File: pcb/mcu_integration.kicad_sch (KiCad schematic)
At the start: 32 parts, among them J5 DM3BT-DSF-PEJS, M1 MountingHole_Pad, M2 MountingHole_Pad, M3 MountingHole_Pad, M4 MountingHole_Pad, U1 STM32F103RBTx, U6 LM35DM, Y1 ECS-80-18-5PX-GM-TR

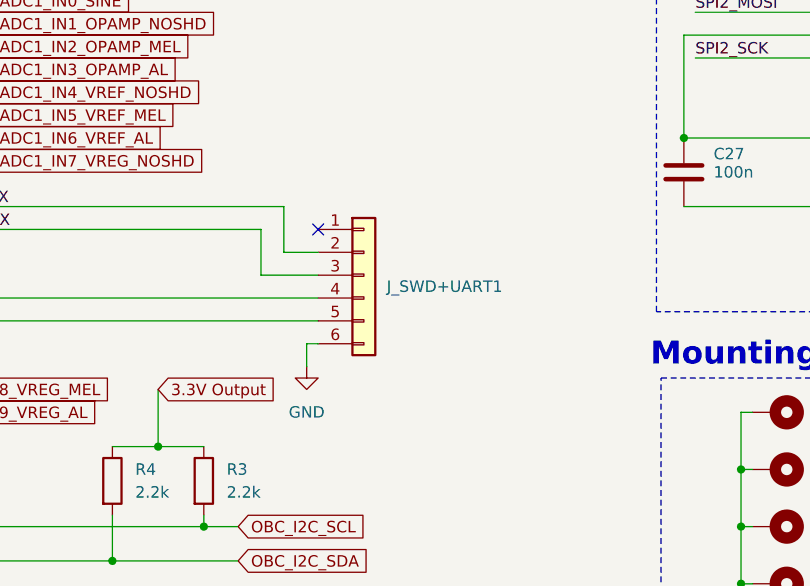
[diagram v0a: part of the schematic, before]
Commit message: Added non-inverting amplifier to RC Ladder and Changed header pin
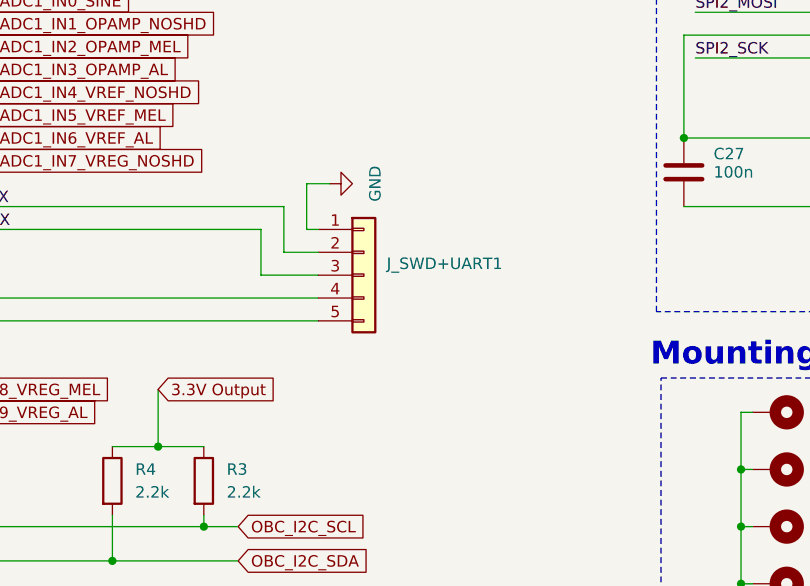
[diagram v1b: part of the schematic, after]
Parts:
- removed J_SWD+UART1: Conn_01x06, Connector_PinHeader_2.54mm:PinHeader_1x06_P2.54mm_Vertical, symbol Connector_Generic:Conn_01x06
- added J_SWD+UART1: J_SWD+UART1, Connector_PinHeader_2.54mm:PinHeader_1x05_P2.54mm_Vertical, symbol Connector_Generic:Conn_01x05
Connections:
- net GND: now also J_SWD+UART1.1 (Pin_1)
- net SWCLK: now also J_SWD+UART1.5 (Pin_5)
- net SWDIO: now also J_SWD+UART1.4 (Pin_4)
- net USART1_RX: now also J_SWD+UART1.3 (Pin_3)
- net USART1_TX: now also J_SWD+UART1.2 (Pin_2)
- no-connect marks 31 -> 30
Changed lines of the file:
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@@
 	)
 	(no_connect
-		(at 163.83 62.23)
-	)
-	(no_connect
 		(at 116.84 105.41)
 	)
@@
 	(wire
 		(pts
-			(xy 162.56 74.93) (xy 163.83 74.93)
-		)
-		(stroke
-			(width 0)
-			(type default)
-		)
-	)
-	(wire
-		(pts
 			(xy 60.96 134.62) (xy 77.47 134.62)
 		)
@@
 	(wire
 		(pts
-			(xy 162.56 77.47) (xy 162.56 74.93)
+			(xy 165.1 57.15) (xy 162.56 57.15)
 		)
 		(stroke
@@
 	(wire
 		(pts
+			(xy 162.56 57.15) (xy 162.56 62.23)
+		)
+		(stroke
+			(width 0)
+			(type default)
+		)
+	)
+	(wire
+		(pts
 			(xy 210.82 82.55) (xy 212.09 82.55)
 		)
@@
 	(wire
 		(pts
+			(xy 163.83 62.23) (xy 162.56 62.23)
+		)
+		(stroke
+			(width 0)
+			(type default)
+		)
+	)
+	(wire
+		(pts
 			(xy 96.52 30.48) (xy 99.06 30.48)
 		)
@@
 	(label "SPI2_SCK"
 		(at 205.74 43.18 0)
-		(fields_autoplaced yes)
 		(effects
 			(font
@@
 	(label "SPI2_CS_NSS"
 		(at 205.74 35.56 0)
-		(fields_autoplaced yes)
 		(effects
 			(font
@@
 	(label "HSE_OSC_OUT"
 		(at 67.31 49.53 0)
-		(fields_autoplaced yes)
 		(effects
 			(font
@@
 	(label "USART1_TX"
 		(at 119.38 59.69 0)
-		(fields_autoplaced yes)
 		(effects
 			(font
@@
 	(label "HSE_OSC_IN"
 		(at 67.31 46.99 0)
-		(fields_autoplaced yes)
 		(effects
 			(font
@@
 	(label "SPI2_CS_NSS"
 		(at 119.38 110.49 0)
-		(fields_autoplaced yes)
 		(effects
 			(font
@@
 	(label "SPI2_MOSI"
 		(at 205.74 38.1 0)
-		(fields_autoplaced yes)
 		(effects
 			(font
@@
 	(label "SPI2_MOSI"
 		(at 119.38 118.11 0)
-		(fields_autoplaced yes)
 		(effects
 			(font
@@
 	(label "SPI2_MISO"
 		(at 119.38 115.57 0)
-		(fields_autoplaced yes)
 		(effects
 			(font
@@
 	(label "SWCLK"
 		(at 119.38 72.39 0)
-		(fields_autoplaced yes)
 		(effects
 			(font
@@
 	(label "USART1_RX"
 		(at 119.38 62.23 0)
-		(fields_autoplaced yes)
 		(effects
 			(font
@@
 	(label "SPI2_MISO"
 		(at 276.86 40.64 180)
-		(fields_autoplaced yes)
 		(effects
 			(font
@@
 	(label "BOOT0"
 		(at 68.58 40.64 0)
-		(fields_autoplaced yes)
 		(effects
 			(font
@@
 	(label "NRST"
 		(at 73.66 36.83 0)
-		(fields_autoplaced yes)
 		(effects
 			(font
@@
 	(label "SWDIO"
 		(at 119.38 69.85 0)
-		(fields_autoplaced yes)
 		(effects
 			(font
@@
 	(label "SPI2_SCK"
 		(at 119.38 113.03 0)
-		(fields_autoplaced yes)
 		(effects
 			(font
@@
 	)
 	(symbol
-		(lib_id "Connector_Generic:Conn_01x06")
-		(at 168.91 67.31 0)
-		(unit 1)
-		(exclude_from_sim no)
-		(in_bom yes)
-		(on_board yes)
-		(dnp no)
-		(fields_autoplaced yes)
-		(property "Reference" "J_SWD+UART1"
-			(at 171.45 68.58 0)
-			(effects
-				(font
-					(size 1.27 1.27)
-				)
-				(justify left)
-			)
-		)
-		(property "Value" "Conn_01x06"
-			(at 171.45 69.85 0)
-			(effects
-				(font
-					(size 1.27 1.27)
-				)
-				(justify left)
-				(hide yes)
-			)
-		)
-		(property "Footprint" "Connector_PinHeader_2.54mm:PinHeader_1x06_P2.54mm_Vertical"
-			(at 168.91 67.31 0)
-			(effects
-				(font
-					(size 1.27 1.27)
-				)
-				(hide yes)
-			)
-		)
-		(property "Datasheet" "~"
-			(at 168.91 67.31 0)
-			(effects
-				(font
-					(size 1.27 1.27)
-				)
-				(hide yes)
-			)
-		)
-		(property "Description" ""
-			(at 168.91 67.31 0)
-			(effects
-				(font
-					(size 1.27 1.27)
-				)
-				(hide yes)
-			)
-		)
-		(pin "1"
-		)
-		(pin "2"
-		)
-		(pin "3"
-		)
-		(pin "4"
-		)
-		(pin "5"
-		)
-		(pin "6"
-		)
-		(instances
-			(project "mcu_integration"
-				(path "/c0210bc3-f67f-47d8-a34e-f002a728adb2"
-					(reference "J_SWD+UART1")
-					(unit 1)
-				)
-			)
-		)
-	)
-	(symbol
 		(lib_id "Device:C")
 		(at 49.53 62.23 180)
@@
 	(symbol
 		(lib_id "power:GND")
-		(at 162.56 77.47 0)
+		(at 165.1 57.15 90)
 		(unit 1)
 		(exclude_from_sim no)
@@
 		(fields_autoplaced yes)
 		(property "Reference" "#PWR013"
-			(at 162.56 83.82 0)
+			(at 171.45 57.15 0)
 			(effects
 				(font
@@
 		)
 		(property "Value" "GND"
-			(at 162.56 82.55 0)
+			(at 170.18 57.15 0)
 			(effects
 				(font
@@
 		)
 		(property "Footprint" ""
-			(at 162.56 77.47 0)
+			(at 165.1 57.15 0)
 			(effects
 				(font
@@
 		)
 		(property "Datasheet" ""
-			(at 162.56 77.47 0)
+			(at 165.1 57.15 0)
 			(effects
 				(font
@@
 		)
 		(property "Description" ""
-			(at 162.56 77.47 0)
+			(at 165.1 57.15 0)
 			(effects
 				(font
@@
 					(unit 1)
 				)
+			)
+		)
+	)
+	(symbol
+		(lib_id "Connector_Generic:Conn_01x05")
+		(at 168.91 67.31 0)
+		(unit 1)
+		(exclude_from_sim no)
+		(in_bom yes)
+		(on_board yes)
+		(dnp no)
+		(property "Reference" "J_SWD+UART1"
+			(at 171.45 66.0399 0)
+			(effects
+				(font
+					(size 1.27 1.27)
+				)
+				(justify left)
+			)
+		)
+		(property "Value" "J_SWD+UART1"
+			(at 171.45 68.58 0)
+			(effects
+				(font
+					(size 1.27 1.27)
+				)
+				(justify left)
+				(hide yes)
+			)
+		)
+		(property "Footprint" "Connector_PinHeader_2.54mm:PinHeader_1x05_P2.54mm_Vertical"
+			(at 168.91 67.31 0)
+			(effects
+				(font
+					(size 1.27 1.27)
+				)
+				(hide yes)
+			)
+		)
+		(property "Datasheet" "~"
+			(at 168.91 67.31 0)
+			(effects
+				(font
+					(size 1.27 1.27)
+				)
+				(hide yes)
+			)
+		)
+		(property "Description" "Generic connector, single row, 01x05, script generated (kicad-library-utils/schlib/autogen/connector/)"
+			(at 168.91 67.31 0)
+			(effects
+				(font
+					(size 1.27 1.27)
+				)
+				(hide yes)
+			)
+		)
+		(pin "1"
+		)
+		(pin "3"
+		)
+		(pin "4"
+		)
+		(pin "2"
+		)
+		(pin "5"
+		)
+		(instances
+			(project "mcu_integration"
+				(path "/c0210bc3-f67f-47d8-a34e-f002a728adb2"
+					(reference "J_SWD+UART1")
+					(unit 1)
+				)

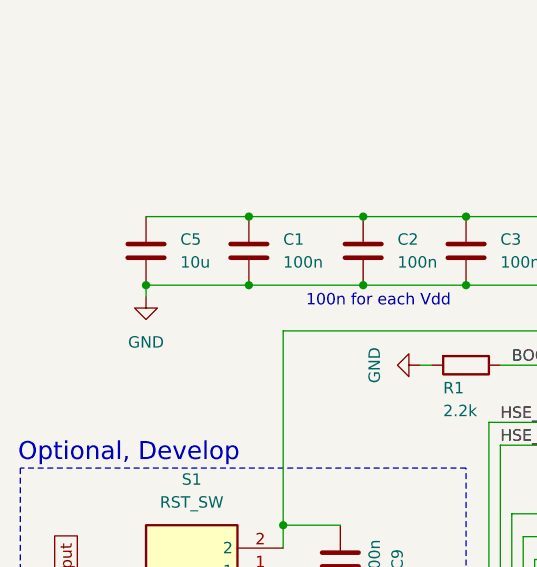
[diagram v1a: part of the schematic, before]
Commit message: Added missing decoupling capacitor + changed capacitors footprint
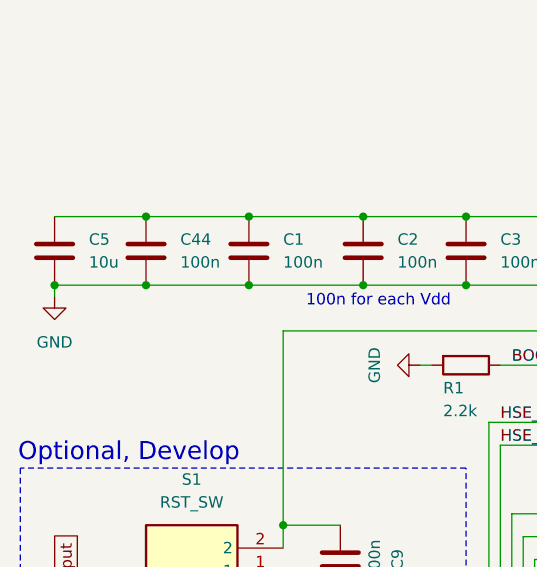
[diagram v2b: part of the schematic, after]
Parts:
- added C44: 100n, Capacitor_SMD:C_0402_1005Metric, symbol Device:C
- C1: footprint Resistor_SMD:R_0402_1005Metric -> Capacitor_SMD:C_0402_1005Metric
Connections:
- net 3.3V Output: now also C44.1
- net GND: now also C44.2
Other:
- moved on the sheet: C5
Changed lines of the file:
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@@
 	)
 	(junction
+		(at 27.94 31.75)
+		(diameter 0)
+		(color 0 0 0 0)
+	)
+	(junction
 		(at 151.13 95.25)
 		(diameter 0)
@@
 	)
 	(junction
-		(at 154.94 20.32)
+		(at 27.94 24.13)
 		(diameter 0)
 		(color 0 0 0 0)
 	)
 	(junction
-		(at 27.94 31.75)
+		(at 154.94 20.32)
 		(diameter 0)
 		(color 0 0 0 0)
@@
 	)
 	(junction
+		(at 17.78 31.75)
+		(diameter 0)
+		(color 0 0 0 0)
+	)
+	(junction
 		(at 44.45 95.25)
 		(diameter 0)
@@
 	(wire
 		(pts
-			(xy 27.94 31.75) (xy 39.37 31.75)
-		)
-		(stroke
-			(width 0)
-			(type default)
-		)
-	)
-	(wire
-		(pts
 			(xy 43.18 63.5) (xy 43.18 66.04)
 		)
@@
 	(wire
 		(pts
-			(xy 27.94 31.75) (xy 27.94 33.02)
+			(xy 17.78 31.75) (xy 17.78 33.02)
 		)
 		(stroke
@@
 	(wire
 		(pts
+			(xy 27.94 31.75) (xy 39.37 31.75)
+		)
+		(stroke
+			(width 0)
+			(type default)
+		)
+	)
+	(wire
+		(pts
 			(xy 160.02 64.77) (xy 163.83 64.77)
 		)
@@
 	(wire
 		(pts
-			(xy 27.94 24.13) (xy 39.37 24.13)
+			(xy 17.78 24.13) (xy 27.94 24.13)
 		)
 		(stroke
@@
 	(wire
 		(pts
+			(xy 27.94 24.13) (xy 39.37 24.13)
+		)
+		(stroke
+			(width 0)
+			(type default)
+		)
+	)
+	(wire
+		(pts
 			(xy 163.83 62.23) (xy 162.56 62.23)
 		)
@@
 	(wire
 		(pts
+			(xy 17.78 31.75) (xy 27.94 31.75)
+		)
+		(stroke
+			(width 0)
+			(type default)
+		)
+	)
+	(wire
+		(pts
 			(xy 204.47 52.07) (xy 222.25 52.07)
 		)
@@
 	(symbol
 		(lib_id "Device:C")
-		(at 27.94 27.94 0)
+		(at 17.78 27.94 0)
 		(unit 1)
 		(exclude_from_sim no)
@@
 		(fields_autoplaced yes)
 		(property "Reference" "C5"
-			(at 31.75 26.67 0)
+			(at 21.59 26.67 0)
 			(effects
 				(font
@@
 		)
 		(property "Value" "10u"
-			(at 31.75 29.21 0)
+			(at 21.59 29.21 0)
 			(effects
 				(font
@@
 		)
 		(property "Footprint" "Capacitor_SMD:C_0603_1608Metric"
-			(at 28.9052 31.75 0)
+			(at 18.7452 31.75 0)
 			(effects
 				(font
@@
 		)
 		(property "Datasheet" "~"
-			(at 27.94 27.94 0)
+			(at 17.78 27.94 0)
 			(effects
 				(font
@@
 		)
 		(property "Description" ""
-			(at 27.94 27.94 0)
+			(at 17.78 27.94 0)
 			(effects
 				(font
@@
 	(symbol
 		(lib_id "Device:C")
+		(at 27.94 27.94 0)
+		(unit 1)
+		(exclude_from_sim no)
+		(in_bom yes)
+		(on_board yes)
+		(dnp no)
+		(fields_autoplaced yes)
+		(property "Reference" "C44"
+			(at 31.75 26.67 0)
+			(effects
+				(font
+					(size 1.27 1.27)
+				)
+				(justify left)
+			)
+		)
+		(property "Value" "100n"
+			(at 31.75 29.21 0)
+			(effects
+				(font
+					(size 1.27 1.27)
+				)
+				(justify left)
+			)
+		)
+		(property "Footprint" "Capacitor_SMD:C_0402_1005Metric"
+			(at 28.9052 31.75 0)
+			(effects
+				(font
+					(size 1.27 1.27)
+				)
+				(hide yes)
+			)
+		)
+		(property "Datasheet" "~"
+			(at 27.94 27.94 0)
+			(effects
+				(font
+					(size 1.27 1.27)
+				)
+				(hide yes)
+			)
+		)
+		(property "Description" ""
+			(at 27.94 27.94 0)
+			(effects
+				(font
+					(size 1.27 1.27)
+				)
+				(hide yes)
+			)
+		)
+		(pin "1"
+		)
+		(pin "2"
+		)
+		(instances
+			(project "mcu_integration"
+				(path "/c0210bc3-f67f-47d8-a34e-f002a728adb2"
+					(reference "C44")
+					(unit 1)
+				)
+			)
+		)
+	)
+	(symbol
+		(lib_id "Device:C")
 		(at 76.2 27.94 0)
 		(unit 1)
@@
 			)
 		)
-		(property "Footprint" "Resistor_SMD:R_0402_1005Metric"
+		(property "Footprint" "Capacitor_SMD:C_0402_1005Metric"
 			(at 40.3352 31.75 0)
 			(effects
@@
 	(symbol
 		(lib_id "power:GND")
-		(at 27.94 33.02 0)
+		(at 17.78 33.02 0)
 		(unit 1)
 		(exclude_from_sim no)
@@
 		(fields_autoplaced yes)
 		(property "Reference" "#PWR03"
-			(at 27.94 39.37 0)
+			(at 17.78 39.37 0)
 			(effects
 				(font
@@
 		)
 		(property "Value" "GND"
-			(at 27.94 38.1 0)
+			(at 17.78 38.1 0)
 			(effects
 				(font
@@
 		)
 		(property "Footprint" ""
-			(at 27.94 33.02 0)
+			(at 17.78 33.02 0)
 			(effects
 				(font
@@
 		)
 		(property "Datasheet" ""
-			(at 27.94 33.02 0)
+			(at 17.78 33.02 0)
 			(effects
 				(font
@@
 		)
 		(property "Description" ""
-			(at 27.94 33.02 0)
+			(at 17.78 33.02 0)
 			(effects
 				(font

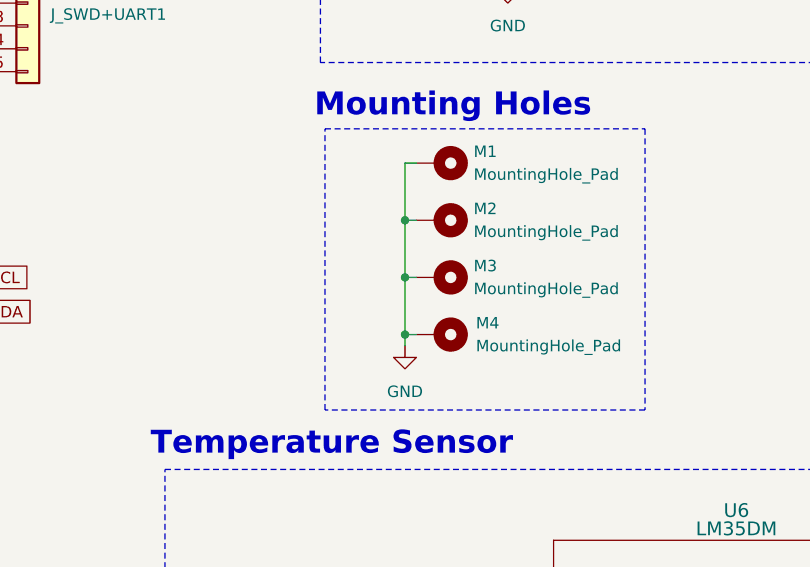
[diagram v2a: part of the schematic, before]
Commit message: Added copper pours to top and bottom layer, added 3.3v plane, spaced ICs to fit melanin caps, ungrounded connection pads, added stitching vias to outer edge
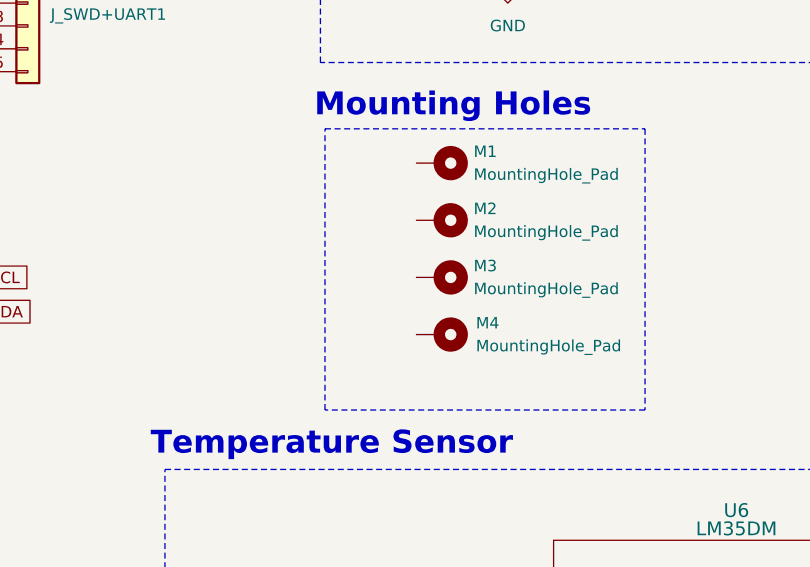
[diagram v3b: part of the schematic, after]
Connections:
- net GND: no longer M1.1, M2.1, M3.1, M4.1

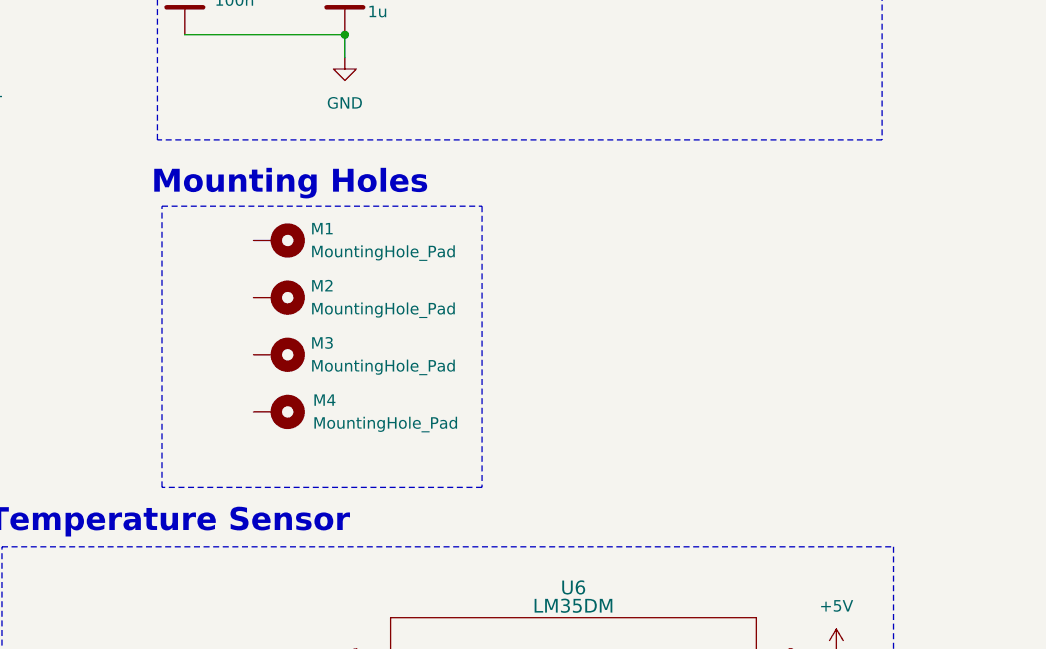
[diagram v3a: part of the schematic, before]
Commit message: Added Shield Footprints
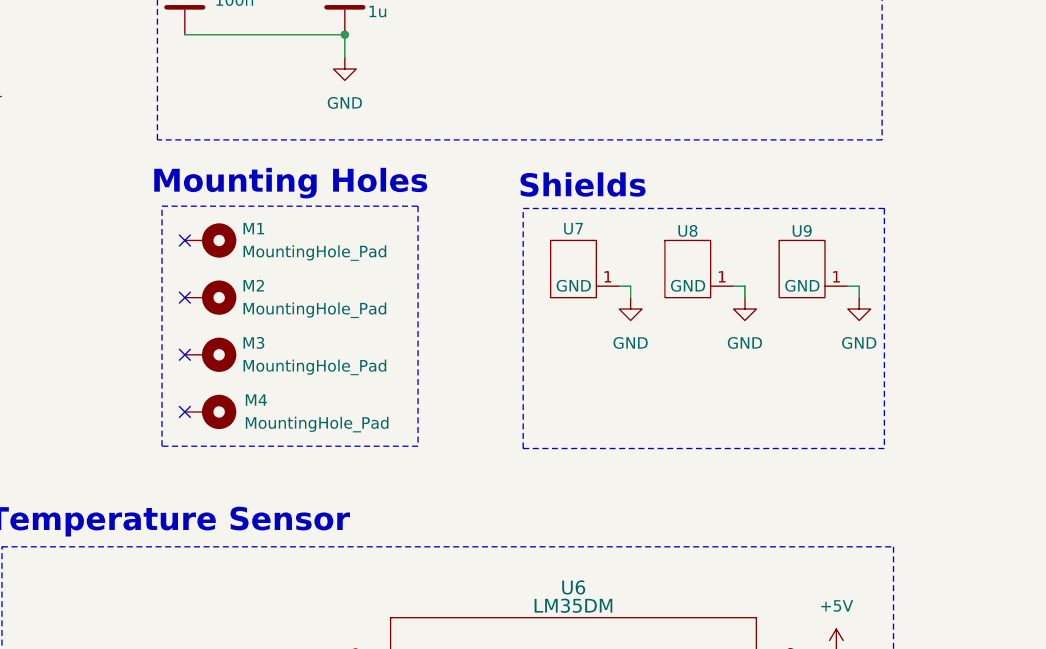
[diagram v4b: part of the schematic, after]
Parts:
- added U7: ~, capstone:AD844 Shield, symbol capstone:AD844_SHIELD
- added U8: ~, capstone:FOD814 Shield, symbol capstone:FOD814_SHIELD
- added U9: ~, capstone:REF192 Shield, symbol capstone:REF192_SHIELD
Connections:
- net GND: now also U7.1 (GND), U8.1 (GND), U9.1 (GND)
- no-connect marks 30 -> 34
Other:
- note added: "Shields"
- moved on the sheet: M1, M2, M3, M4
